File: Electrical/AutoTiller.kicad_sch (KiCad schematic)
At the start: 13 parts, among them J3 T4145415031-001, U5 BHTGA-A-DW, U6 VO615A-4

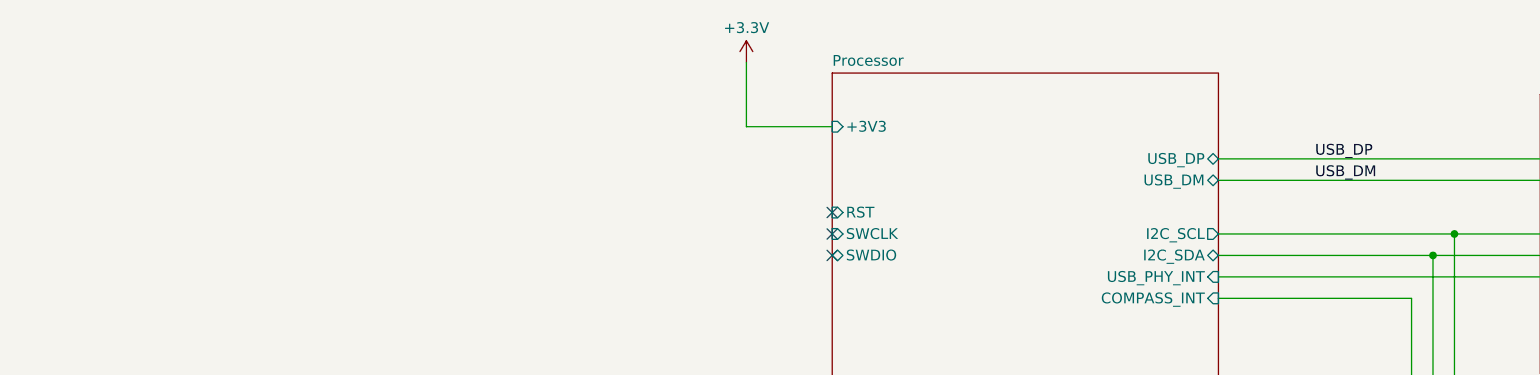
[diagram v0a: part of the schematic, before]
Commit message: Added layout for prototype 1
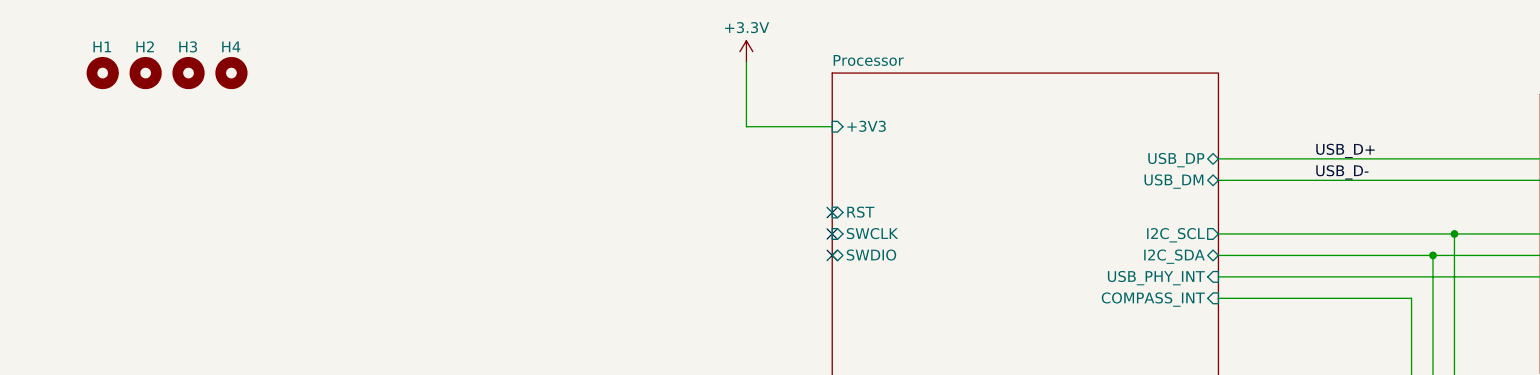
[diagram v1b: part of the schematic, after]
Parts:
- added H1, H2, H3, H4: MountingHole, MountingHole:MountingHole_3.2mm_M3_DIN965_Pad_TopBottom, symbol Mechanical:MountingHole
- U5: footprint (none) -> Connector_PinHeader_2.54mm:PinHeader_1x05_P2.54mm_Vertical; now left out of the parts list
